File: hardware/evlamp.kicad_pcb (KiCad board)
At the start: 2 copper layers, 56 x 63 mm, 25 parts, among them X1 LED 0, X10 DOWN, X11 MAIN, X2 LED 1, X3 LED 2, X4 LED 3, X5 LED 4, X6 LED 5, X7 LED 6, X8 LED 7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

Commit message: update KiCad project
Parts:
- added C2: 470,0 6,3V, Capacitor_Tantalum_SMD:CP_EIA-7343-31_Kemet-D_Pad2.25x2.55mm_HandSolder, F.Cu at (76.5, 114.8)
- X10: value DOWN -> "DOWN"
- X11: value MAIN -> "MAIN"
- X9: value UP -> "UP"
- moved C1 3.60 mm to (87.6, 78.3), turned to 90 degrees
- moved REF** 3.00 mm to (76.5, 126.2)
- moved REF** 3.00 mm to (114.5, 126.2)
- moved X6 2.36 mm to (108.0, 126.2)
- moved X7 2.36 mm to (97.8, 126.2)
- moved X8 2.36 mm to (87.6, 126.2)
- moved X1 0.54 mm to (123.5, 74.7)
- moved X2 0.54 mm to (123.5, 89.9)
- moved X3 0.54 mm to (123.5, 100.1)
- moved X4 0.54 mm to (123.5, 110.3)
- moved X5 0.54 mm to (123.5, 120.4)
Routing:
- net +5V: track 81.6 -> 86.2 mm
- net Net-(C1-Pad2): track 3.68 -> 6.13 mm
- net Net-(R8-Pad2): track 54.0 -> 51.7 mm
- net Net-(R7-Pad2): track 51.2 -> 48.8 mm
- net Net-(R6-Pad2): track 17.9 -> 15.6 mm
- net Net-(R4-Pad2): track 13.0 -> 12.4 mm
- net Net-(R3-Pad2): track 9.82 -> 9.28 mm
- net Net-(R2-Pad2): track 13.0 -> 12.4 mm
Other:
- board size 56 x 63 mm -> 55 x 60 mm

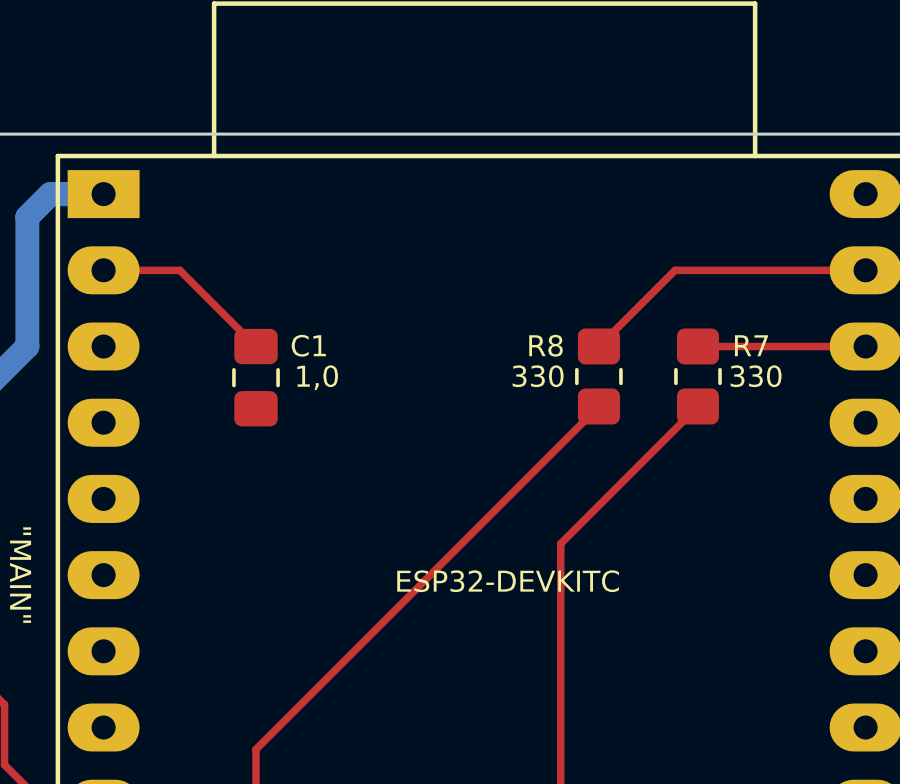
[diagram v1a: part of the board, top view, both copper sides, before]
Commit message: add checkbox support to effect parameters
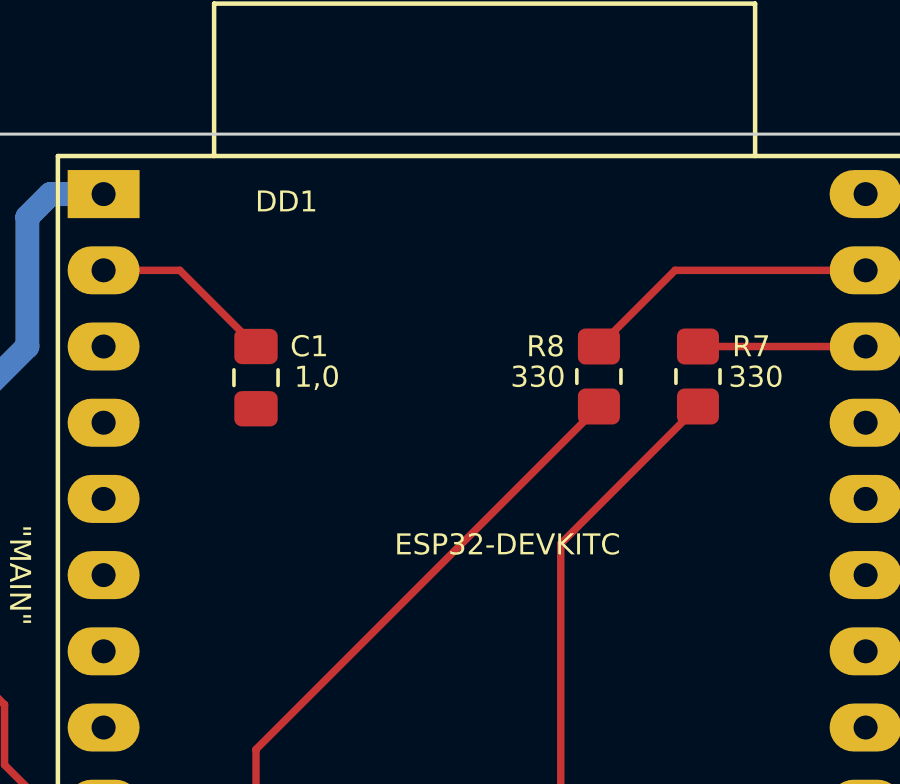
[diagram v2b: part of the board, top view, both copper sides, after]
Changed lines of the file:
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@@
     (property "Sheetname" "")
     (attr through_hole)
-    (fp_text reference "DD1" (at 6.096 0.254 unlocked) (layer "F.SilkS") hide
+    (fp_text reference "DD1" (at 6.096 0.254 unlocked) (layer "F.SilkS")
       (effects (font (size 0.7 0.7) (thickness 0.15)))
     )
-    (fp_text value "ESP32-DEVKITC" (at 13.462 12.929 unlocked) (layer "F.SilkS")
+    (fp_text value "ESP32-DEVKITC" (at 13.462 11.684 unlocked) (layer "F.SilkS")
       (effects (font (size 0.7 0.7) (thickness 0.15)))
     )
-    (fp_text user "${REFERENCE}" (at 7.62 24.13 unlocked) (layer "F.Fab")
+    (fp_text user "${REFERENCE}" (at 7.62 24.13) (layer "F.Fab")
       (effects (font (size 1 1) (thickness 0.15)))
     )
+    (fp_line (start 3.683 -6.35) (end 21.717 -6.35) (layer "F.SilkS") (width 0.15))
+    (fp_line (start -1.524 -1.27) (end -1.524 46.99) (layer "F.SilkS") (width 0.15))
     (fp_line (start 21.717 -6.35) (end 21.717 -1.27) (layer "F.SilkS") (width 0.15))
-    (fp_line (start 3.683 -6.35) (end 21.717 -6.35) (layer "F.SilkS") (width 0.15))
+    (fp_line (start 26.924 -1.27) (end -1.524 -1.27) (layer "F.SilkS") (width 0.15))
     (fp_line (start -1.524 46.99) (end 26.924 46.99) (layer "F.SilkS") (width 0.15))
+    (fp_line (start 26.924 46.99) (end 26.924 -1.27) (layer "F.SilkS") (width 0.15))
     (fp_line (start 3.683 -6.35) (end 3.683 -1.27) (layer "F.SilkS") (width 0.15))
-    (fp_line (start 26.924 -1.27) (end -1.524 -1.27) (layer "F.SilkS") (width 0.15))
-    (fp_line (start 26.924 46.99) (end 26.924 -1.27) (layer "F.SilkS") (width 0.15))
-    (fp_line (start -1.524 -1.27) (end -1.524 46.99) (layer "F.SilkS") (width 0.15))
     (fp_line (start 26.924 48.006) (end -1.524 48.006) (layer "F.CrtYd") (width 0.05))
     (fp_line (start 26.924 -6.35) (end 26.924 48.006) (layer "F.CrtYd") (width 0.05))

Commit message: update to ver 0.7.4
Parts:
- moved C1 1.53 mm to (86.5, 77.2), turned to 180 degrees
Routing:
- net Net-(C1-Pad2): track 6.13 -> 4.69 mm
